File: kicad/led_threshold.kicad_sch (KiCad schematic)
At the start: 16 parts, among them Q1 2N7002E, Q2 2N7002E, SW5 EG6100-ND, U21 OPA189, U22 4x Comparator

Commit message: Fixed Digikey Part numbers for some parts, confirmed final BOM, Fixed Switch Footprint hole size
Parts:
- C25: DIGIKEY 1276-6840-2-ND -> 1276-6840-1-ND
- D3: DIGIKEY 160-2033-2-ND -> 160-2033-1-ND
- Q1, Q2: DIGIKEY 2N7002BK,215 -> 1727-4789-1-ND
- R11: DIGIKEY P100KDATR-ND -> P100KDACT-ND
- R28: DIGIKEY 5831-2-2176327-5TR-ND -> RG20P1.0KBCT-ND; PARTNO 2-2176327-5 -> RG2012P-102-B-T5
- R32, R39: DIGIKEY P16057TR-ND -> P16057CT-ND
- U22: DIGIKEY UPC177G2(20)-E2-A -> 559-UPC177G2(20)-E2-ACT-ND
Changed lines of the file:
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@@
 			)
 		)
-		(property "DIGIKEY" "UPC177G2(20)-E2-A"
+		(property "DIGIKEY" "559-UPC177G2(20)-E2-ACT-ND"
 			(at 172.72 97.79 0)
 			(effects
@@
 			)
 		)
-		(property "DIGIKEY" "2N7002BK,215"
+		(property "DIGIKEY" "1727-4789-1-ND"
 			(at 228.6 48.26 90)
 			(effects
@@
 			)
 		)
-		(property "DIGIKEY" "P100KDATR-ND"
+		(property "DIGIKEY" "P100KDACT-ND"
 			(at 44.45 43.18 0)
 			(effects
@@
 			)
 		)
-		(property "DIGIKEY" "UPC177G2(20)-E2-A"
+		(property "DIGIKEY" "559-UPC177G2(20)-E2-ACT-ND"
 			(at 129.54 60.96 0)
 			(effects
@@
 			)
 		)
-		(property "DIGIKEY" "P16057TR-ND"
+		(property "DIGIKEY" "P16057CT-ND"
 			(at 228.6 38.1 0)
 			(effects
@@
 			)
 		)
-		(property "DIGIKEY" "UPC177G2(20)-E2-A"
+		(property "DIGIKEY" "559-UPC177G2(20)-E2-ACT-ND"
 			(at 116.84 31.75 0)
 			(effects
@@
 			)
 		)
-		(property "DIGIKEY" "P16057TR-ND"
+		(property "DIGIKEY" "P16057CT-ND"
 			(at 214.63 92.71 0)
 			(effects
@@
 			)
 		)
-		(property "DIGIKEY" "5831-2-2176327-5TR-ND"
+		(property "DIGIKEY" "RG20P1.0KBCT-ND"
 			(at 166.37 46.99 90)
 			(effects
@@
 			)
 		)
-		(property "PARTNO" "2-2176327-5"
+		(property "PARTNO" "RG2012P-102-B-T5"
 			(at 166.37 46.99 90)
 			(effects
@@
 			)
 		)
-		(property "DIGIKEY" "160-2033-2-ND"
+		(property "DIGIKEY" "160-2033-1-ND"
 			(at 205.74 66.04 0)
 			(effects
@@
 			)
 		)
-		(property "DIGIKEY" "1276-6840-2-ND "
+		(property "DIGIKEY" "1276-6840-1-ND "
 			(at 53.34 64.77 90)
 			(effects
@@
 			)
 		)
-		(property "DIGIKEY" "UPC177G2(20)-E2-A"
+		(property "DIGIKEY" "559-UPC177G2(20)-E2-ACT-ND"
 			(at 142.24 127 0)
 			(effects
@@
 			)
 		)
-		(property "DIGIKEY" "2N7002BK,215"
+		(property "DIGIKEY" "1727-4789-1-ND"
 			(at 214.63 82.55 90)
 			(effects

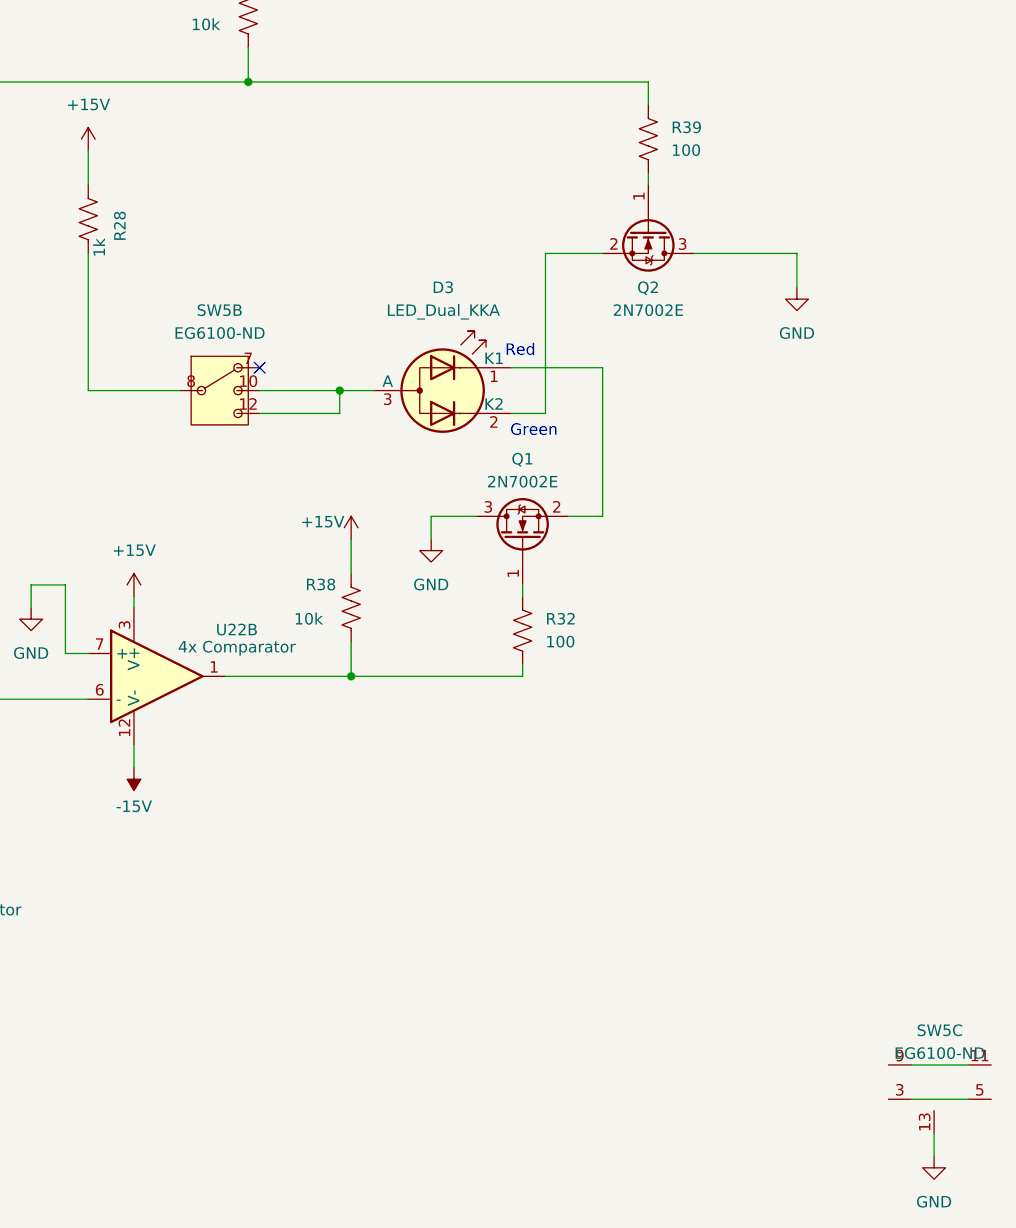
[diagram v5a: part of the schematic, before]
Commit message: V1.1, Fixedincorrect footprints for Green/Red LED, Diodes, Mosfets, Flipped Input A/B Polarity, Potentiometer labels, Incorrect part nos for V regulators. No functionality changes
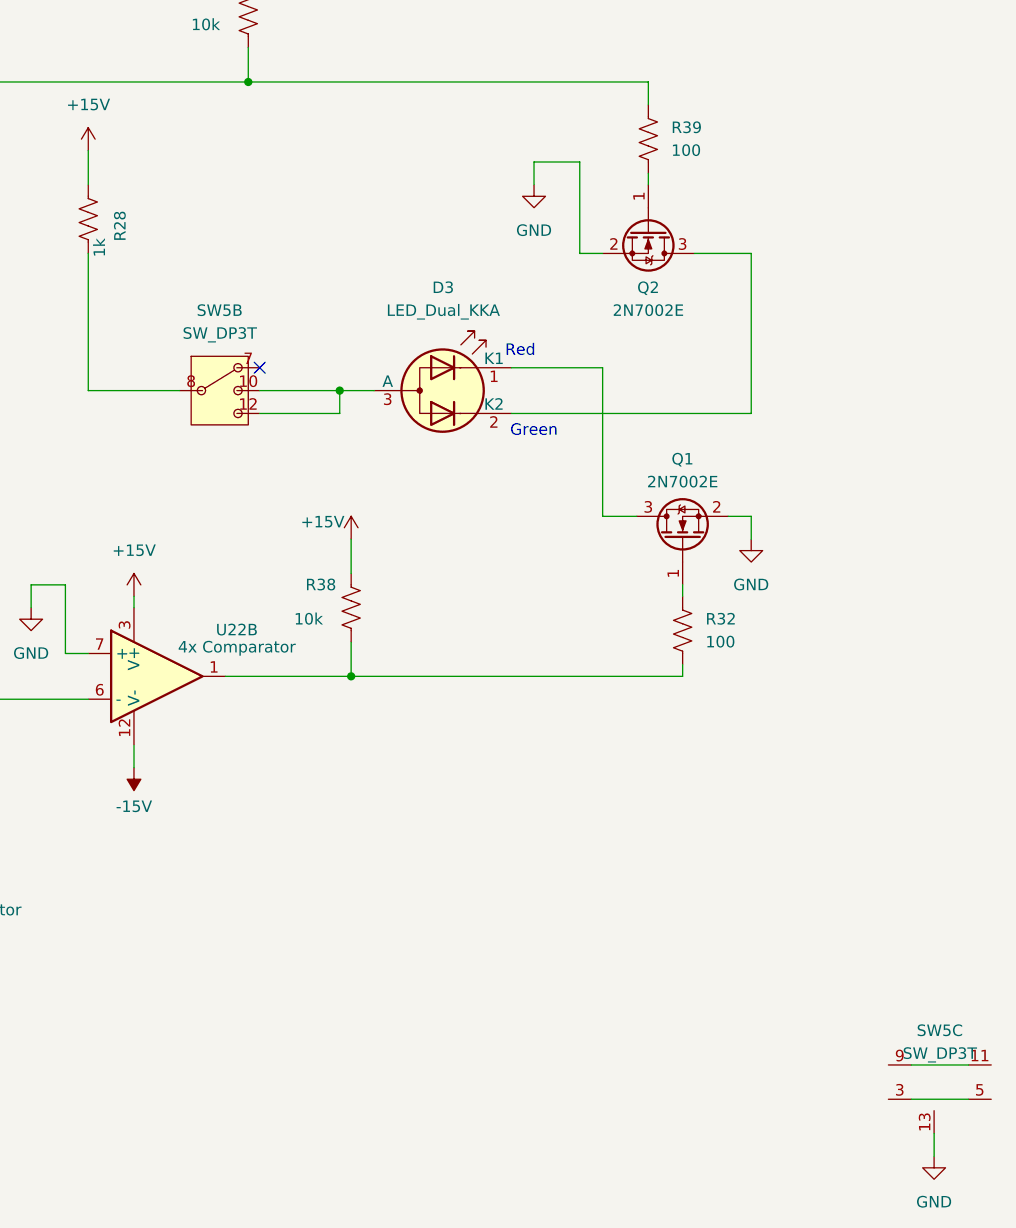
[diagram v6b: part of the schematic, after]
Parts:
- SW5: value EG6100-ND -> SW_DP3T
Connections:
- net GND: now also Q1.2 (S), Q2.2 (S); no longer Q1.3 (D), Q2.3 (D)
- net at D3.2 (K2): now also Q2.3 (D); no longer Q2.2 (S)
- net at D3.1 (K1): now also Q1.3 (D); no longer Q1.2 (S)
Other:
- moved on the sheet: Q1, R32
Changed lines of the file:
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@@
 	(wire
 		(pts
-			(xy 217.17 50.8) (xy 223.52 50.8)
+			(xy 215.9 40.64) (xy 215.9 43.18)
 		)
 		(stroke
@@
 	(wire
 		(pts
+			(xy 237.49 80.01) (xy 240.03 80.01)
+		)
+		(stroke
+			(width 0)
+			(type default)
+		)
+	)
+	(wire
+		(pts
 			(xy 93.98 82.55) (xy 87.63 82.55)
 		)
@@
 	(wire
 		(pts
-			(xy 166.37 66.04) (xy 176.53 66.04)
+			(xy 223.52 50.8) (xy 220.98 50.8)
 		)
 		(stroke
@@
 	(wire
 		(pts
-			(xy 233.68 50.8) (xy 245.11 50.8)
+			(xy 166.37 66.04) (xy 176.53 66.04)
 		)
 		(stroke
@@
 	(wire
 		(pts
-			(xy 228.6 31.75) (xy 228.6 34.29)
+			(xy 223.52 80.01) (xy 227.33 80.01)
 		)
 		(stroke
@@
 	(wire
 		(pts
-			(xy 213.36 63.5) (xy 223.52 63.5)
+			(xy 228.6 31.75) (xy 228.6 34.29)
 		)
 		(stroke
@@
 	(wire
 		(pts
-			(xy 217.17 50.8) (xy 217.17 68.58)
+			(xy 213.36 63.5) (xy 223.52 63.5)
 		)
 		(stroke
@@
 	(wire
 		(pts
-			(xy 204.47 80.01) (xy 204.47 82.55)
+			(xy 240.03 80.01) (xy 240.03 82.55)
 		)
 		(stroke
@@
 	(wire
 		(pts
-			(xy 257.81 144.78) (xy 264.16 144.78)
+			(xy 220.98 40.64) (xy 215.9 40.64)
 		)
 		(stroke
@@
 	(wire
 		(pts
-			(xy 181.61 97.79) (xy 195.58 97.79)
-		)
-		(stroke
-			(width 0)
-			(type default)
-		)
-	)
-	(wire
-		(pts
-			(xy 125.73 31.75) (xy 154.94 31.75)
+			(xy 257.81 144.78) (xy 264.16 144.78)
 		)
 		(stroke
@@
 	(wire
 		(pts
-			(xy 71.12 29.21) (xy 71.12 58.42)
+			(xy 181.61 97.79) (xy 195.58 97.79)
 		)
 		(stroke
@@
 	(wire
 		(pts
-			(xy 257.81 140.97) (xy 264.16 140.97)
+			(xy 125.73 31.75) (xy 154.94 31.75)
 		)
 		(stroke
@@
 	(wire
 		(pts
-			(xy 223.52 80.01) (xy 219.71 80.01)
+			(xy 71.12 29.21) (xy 71.12 58.42)
 		)
 		(stroke
@@
 	(wire
 		(pts
-			(xy 214.63 97.79) (xy 214.63 96.52)
+			(xy 257.81 140.97) (xy 264.16 140.97)
 		)
 		(stroke
@@
 	(wire
 		(pts
+			(xy 232.41 97.79) (xy 232.41 96.52)
+		)
+		(stroke
+			(width 0)
+			(type default)
+		)
+	)
+	(wire
+		(pts
 			(xy 195.58 86.36) (xy 195.58 82.55)
 		)
@@
 	(wire
 		(pts
-			(xy 214.63 88.9) (xy 214.63 87.63)
+			(xy 232.41 88.9) (xy 232.41 87.63)
+		)
+		(stroke
+			(width 0)
+			(type default)
+		)
+	)
+	(wire
+		(pts
+			(xy 240.03 50.8) (xy 233.68 50.8)
 		)
 		(stroke
@@
 	(wire
 		(pts
-			(xy 223.52 63.5) (xy 223.52 80.01)
+			(xy 240.03 68.58) (xy 240.03 50.8)
 		)
 		(stroke
@@
 	(wire
 		(pts
-			(xy 185.42 66.04) (xy 194.31 66.04)
+			(xy 223.52 63.5) (xy 223.52 80.01)
 		)
 		(stroke
@@
 	(wire
 		(pts
-			(xy 53.34 58.42) (xy 53.34 60.96)
+			(xy 185.42 66.04) (xy 194.31 66.04)
 		)
 		(stroke
@@
 	(wire
 		(pts
-			(xy 44.45 34.29) (xy 44.45 39.37)
+			(xy 53.34 58.42) (xy 53.34 60.96)
 		)
 		(stroke
@@
 	(wire
 		(pts
-			(xy 154.94 31.75) (xy 154.94 60.96)
+			(xy 44.45 34.29) (xy 44.45 39.37)
 		)
 		(stroke
@@
 	(wire
 		(pts
-			(xy 209.55 80.01) (xy 204.47 80.01)
+			(xy 154.94 31.75) (xy 154.94 60.96)
 		)
 		(stroke
@@
 	(wire
 		(pts
-			(xy 214.63 97.79) (xy 195.58 97.79)
+			(xy 195.58 97.79) (xy 232.41 97.79)
 		)
 		(stroke
@@
 	(wire
 		(pts
-			(xy 245.11 50.8) (xy 245.11 54.61)
+			(xy 123.19 63.5) (xy 123.19 85.09)
 		)
 		(stroke
@@
 	(wire
 		(pts
-			(xy 123.19 63.5) (xy 123.19 85.09)
+			(xy 105.41 104.14) (xy 123.19 104.14)
 		)
 		(stroke
@@
 	(wire
 		(pts
-			(xy 105.41 104.14) (xy 123.19 104.14)
+			(xy 185.42 68.58) (xy 194.31 68.58)
 		)
 		(stroke
@@
 	(wire
 		(pts
-			(xy 185.42 68.58) (xy 194.31 68.58)
+			(xy 184.15 31.75) (xy 228.6 31.75)
 		)
 		(stroke
@@
 	(wire
 		(pts
-			(xy 184.15 31.75) (xy 228.6 31.75)
+			(xy 220.98 50.8) (xy 220.98 40.64)
 		)
 		(stroke
@@
 	(wire
 		(pts
-			(xy 213.36 68.58) (xy 217.17 68.58)
+			(xy 213.36 68.58) (xy 240.03 68.58)
 		)
 		(stroke
@@
 			)
 		)
-		(property "Value" "EG6100-ND"
+		(property "Value" "SW_DP3T"
 			(at 180.975 59.69 0)
 			(effects
@@
 		(lib_name "GND_2")
 		(lib_id "power:GND")
-		(at 204.47 82.55 0)
+		(at 240.03 82.55 0)
 		(unit 1)
 		(exclude_from_sim no)
@@
 		(fields_autoplaced yes)
 		(property "Reference" "#PWR076"
-			(at 204.47 88.9 0)
+			(at 240.03 88.9 0)
 			(effects
 				(font
@@
 		)
 		(property "Value" "GND"
-			(at 204.47 87.63 0)
+			(at 240.03 87.63 0)
 			(effects
 				(font
@@
 		)
 		(property "Footprint" ""
-			(at 204.47 82.55 0)
+			(at 240.03 82.55 0)
 			(effects
 				(font
@@
 		)
 		(property "Datasheet" ""
-			(at 204.47 82.55 0)
+			(at 240.03 82.55 0)
 			(effects
 				(font
@@
 		)
 		(property "Description" "Power symbol creates a global label with name \"GND\" , ground"
-			(at 204.47 82.55 0)
+			(at 240.03 82.55 0)
 			(effects
 				(font
@@
 			)
 		)
-		(property "Value" "EG6100-ND"
+		(property "Value" "SW_DP3T"
 			(at 260.985 139.7 0)
 			(effects
@@
 	(symbol
 		(lib_id "Device:R_US")
-		(at 214.63 92.71 0)
+		(at 232.41 92.71 0)
 		(unit 1)
 		(exclude_from_sim no)
@@
 		(fields_autoplaced yes)
 		(property "Reference" "R32"
-			(at 217.17 91.4399 0)
+			(at 234.95 91.4399 0)
 			(effects
 				(font
@@
 		)
 		(property "Value" "100"
-			(at 217.17 93.9799 0)
+			(at 234.95 93.9799 0)
 			(effects
 				(font
@@
 		)
 		(property "Footprint" "Resistor_SMD:R_0805_2012Metric"
-			(at 215.646 92.964 90)
+			(at 233.426 92.964 90)
 			(effects
 				(font
@@
 		)
 		(property "Datasheet" "~"
-			(at 214.63 92.71 0)
+			(at 232.41 92.71 0)
 			(effects
 				(font
@@
 		)
 		(property "Description" "Resistor, US symbol"
-			(at 214.63 92.71 0)
+			(at 232.41 92.71 0)
 			(effects
 				(font
@@
 		)
 		(property "DIGIKEY" "P16057CT-ND"
-			(at 214.63 92.71 0)
+			(at 232.41 92.71 0)
 			(effects
 				(font
@@
 		)
 		(property "PARTNO" "ERJ-P06F1000V"
-			(at 214.63 92.71 0)
+			(at 232.41 92.71 0)
 			(effects
 				(font
@@
 		(lib_name "GND_1")
 		(lib_id "power:GND")
-		(at 245.11 54.61 0)
+		(at 215.9 43.18 0)
 		(unit 1)
 		(exclude_from_sim no)
@@
 		(fields_autoplaced yes)
 		(property "Reference" "#PWR075"
-			(at 245.11 60.96 0)
+			(at 215.9 49.53 0)
 			(effects
 				(font
@@
 		)
 		(property "Value" "GND"
-			(at 245.11 59.69 0)
+			(at 215.9 48.26 0)
 			(effects
 				(font
@@
 		)
 		(property "Footprint" ""
-			(at 245.11 54.61 0)
+			(at 215.9 43.18 0)
 			(effects
 				(font
@@
 		)
 		(property "Datasheet" ""
-			(at 245.11 54.61 0)
+			(at 215.9 43.18 0)
 			(effects
 				(font
@@
 		)
 		(property "Description" "Power symbol creates a global label with name \"GND\" , ground"
-			(at 245.11 54.61 0)
+			(at 215.9 43.18 0)
 			(effects
 				(font
@@
 	(symbol
 		(lib_id "Transistor_FET:2N7002E")
-		(at 214.63 82.55 90)
+		(at 232.41 82.55 90)
 		(unit 1)
 		(exclude_from_sim no)
@@
 		(fields_autoplaced yes)
 		(property "Reference" "Q1"
-			(at 214.63 73.66 90)
+			(at 232.41 73.66 90)
 			(effects
 				(font
@@
 		)
 		(property "Value" "2N7002E"
-			(at 214.63 76.2 90)
+			(at 232.41 76.2 90)
 			(effects
 				(font
@@
 		)
 		(property "Footprint" "Package_TO_SOT_SMD:SOT-23"
-			(at 216.535 77.47 0)
+			(at 234.315 77.47 0)
 			(effects
 				(font
@@
 		)
 		(property "Datasheet" "http://www.diodes.com/assets/Datasheets/ds30376.pdf"
-			(at 218.44 77.47 0)
+			(at 236.22 77.47 0)
 			(effects
 				(font
@@
 		)
 		(property "Description" "0.24A Id, 60V Vds, N-Channel MOSFET, SOT-23"
-			(at 214.63 82.55 0)
+			(at 232.41 82.55 0)
 			(effects
 				(font
@@
 		)
 		(property "DIGIKEY" "1727-4789-1-ND"
-			(at 214.63 82.55 90)
+			(at 232.41 82.55 90)
 			(effects
 				(font
@@
 		)
 		(property "PARTNO" "2N7002BK,215"
-			(at 214.63 82.55 90)
+			(at 232.41 82.55 90)
 			(effects
 				(font

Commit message: First pass at schematic for updated bidirectional clamping and output offset when the lock is turned off, no layout changes yet
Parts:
- added R55: 10k, Resistor_SMD:R_0805_2012Metric, symbol Device:R_US
- added U34: TMUX6123, Package_SO:VSSOP-10_3x3mm_P0.5mm, symbol library_intensity_pi:TMUX6123_split
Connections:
- net GND: now also R55.1
- net at SW5.7: now also R55.2, U34.1 (SEL1), U34.10 (SEL2)
- no-connect marks 2 -> 1

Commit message: Updated schematic and design
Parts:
- removed R55: 10k, Resistor_SMD:R_0805_2012Metric, symbol Device:R_US
- removed unit 2 of SW5
- removed U34: TMUX6123, Package_SO:VSSOP-10_3x3mm_P0.5mm, symbol library_intensity_pi:TMUX6123_split
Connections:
- net at D3.3 (A): now also R28.2
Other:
- moved on the sheet: R28
